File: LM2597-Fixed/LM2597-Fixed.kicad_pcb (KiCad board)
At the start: 2 copper layers, 19.6 x 32.4 mm, 9 parts, among them IC1 LM2597MX-5.0_NOPB, J1 Conn_01x03

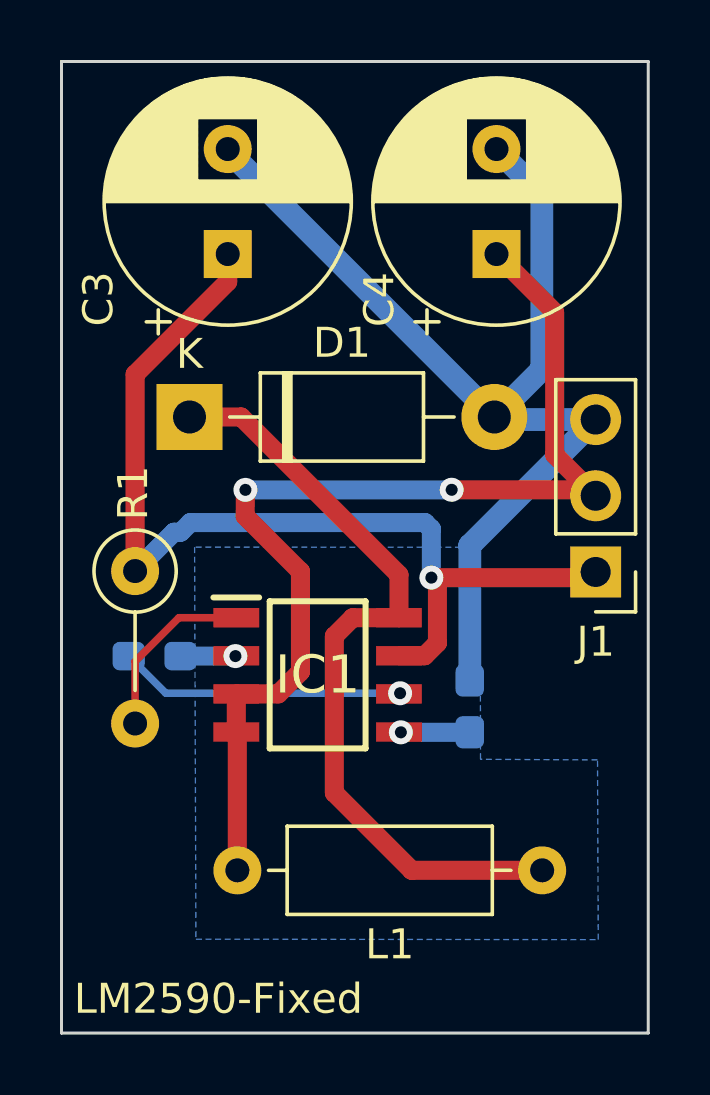
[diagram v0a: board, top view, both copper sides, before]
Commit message: updated all of these to SMD parts
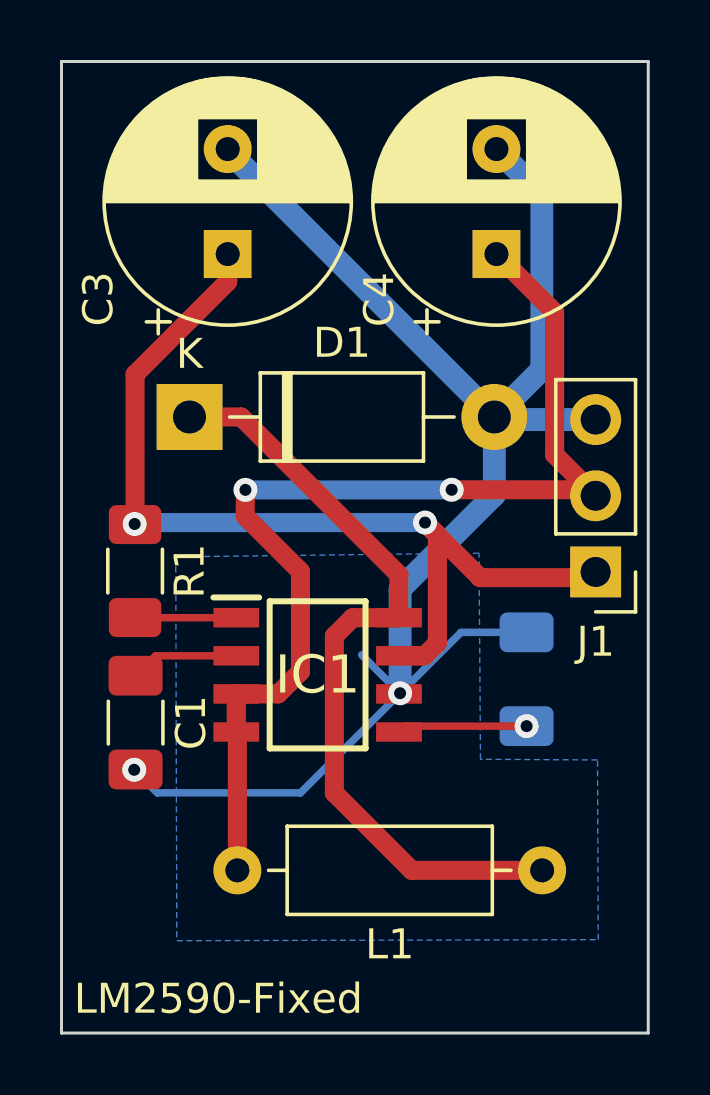
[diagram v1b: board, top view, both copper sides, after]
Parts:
- C1: footprint Capacitor_SMD:C_0603_1608Metric_Pad1.08x0.95mm_HandSolder -> Capacitor_SMD:C_1206_3216Metric_Pad1.33x1.80mm_HandSolder; moved to F.Cu
- C2: footprint Capacitor_SMD:C_0603_1608Metric_Pad1.08x0.95mm_HandSolder -> Capacitor_SMD:C_1206_3216Metric_Pad1.33x1.80mm_HandSolder
- R1: footprint Resistor_THT:R_Axial_DIN0207_L6.3mm_D2.5mm_P5.08mm_Vertical -> Resistor_SMD:R_1206_3216Metric_Pad1.30x1.75mm_HandSolder
- moved C1 2.31 mm to (147.8, 102.1), turned to -90 degrees
- moved C2 2.10 mm to (160.8, 100.7)
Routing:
- net GND: track 46.1 -> 54.0 mm, vias 1 -> 2
- net Net-(IC1-ERROR_FLAG): track 6.04 -> 3.37 mm
- net Net-(IC1-~{SHUTDOWN}/SOFT-START): track 2.30 -> 4.34 mm
- net Net-(IC1-DELAY): track 1.83 -> 3.63 mm, vias 1 -> 0
- net +VDC: track 33.1 -> 31.9 mm, vias 1 -> 2
